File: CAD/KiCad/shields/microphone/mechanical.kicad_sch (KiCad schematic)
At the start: 2 parts

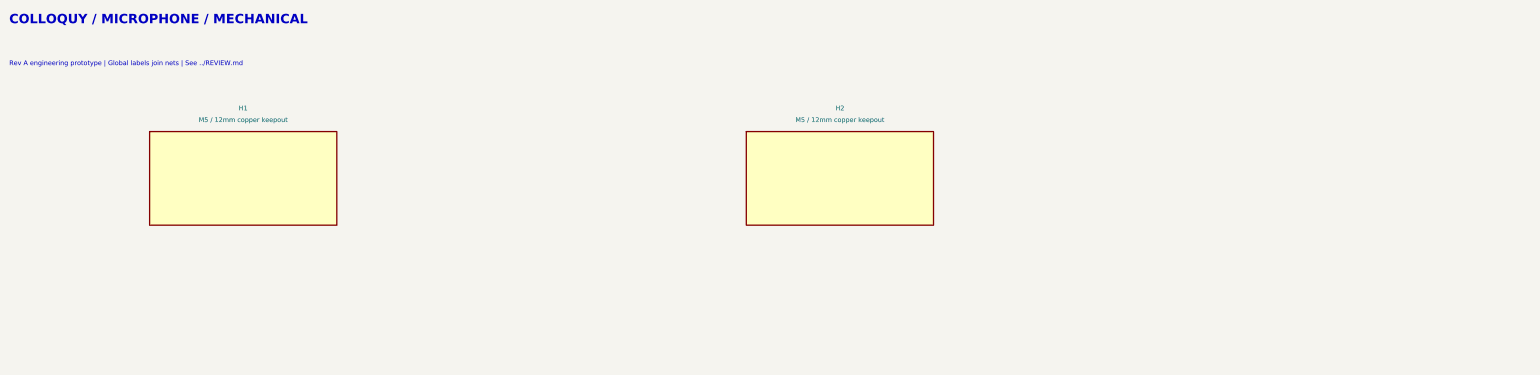
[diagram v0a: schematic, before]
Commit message: Mount the MAX9814 module on a socketed artwork holder
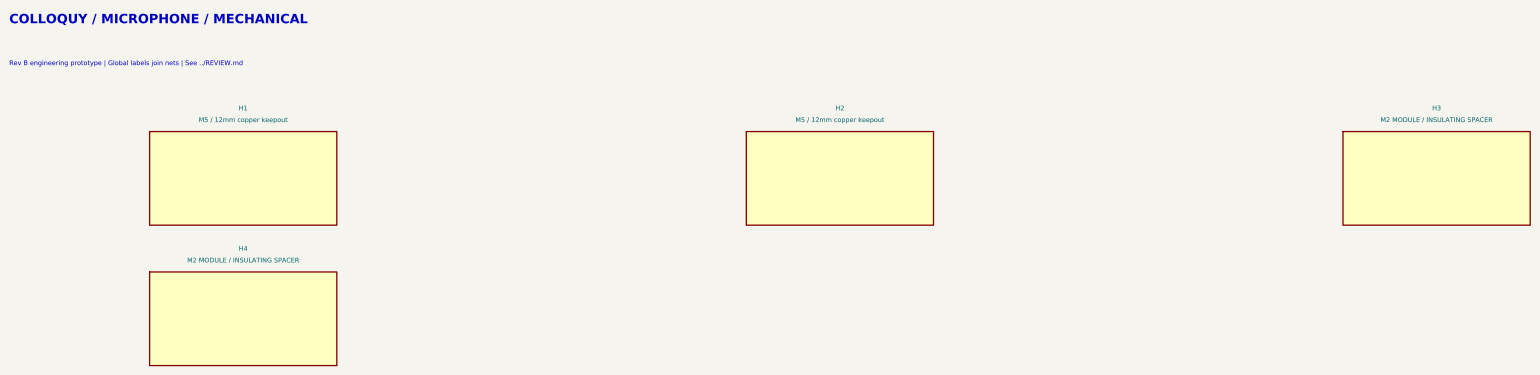
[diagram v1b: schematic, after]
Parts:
- added H3: M2 MODULE / INSULATING SPACER, Shields:MountingHole_2.2mm_M2_Keepout6, symbol Colloquy:H3
- added H4: M2 MODULE / INSULATING SPACER, Shields:MountingHole_2.2mm_M2_Keepout6, symbol Colloquy:H4
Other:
- note added: "Rev B engineering prototype | Global labels join nets | See ../REVIEW.md"
- note removed: "Rev A engineering prototype | Global labels join nets | See ../REVIEW.md"
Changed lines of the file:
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@@
 (kicad_sch (version 20250114) (generator "eeschema") (generator_version "9.0")
  (paper "A3")
-          (title_block (title "microphone / mechanical") (date "2026-10-05") (rev "A-prototype")
+          (title_block (title "microphone / mechanical") (date "2026-10-08") (rev "B-module-holder")
             (company "Colloquy of Mobiles") (comment 1 "Prototype: verify harness polarity and sensor values before connection"))
           (text "COLLOQUY / MICROPHONE / MECHANICAL" (at 15.24 15.24 0) (effects (font (size 2.032 2.032) (bold yes)) (justify left top)))
-(text "Rev A engineering prototype | Global labels join nets | See ../REVIEW.md" (at 15.24 25.4 0) (effects (font (size 1.016 1.016) ) (justify left top)))
+(text "Rev B engineering prototype | Global labels join nets | See ../REVIEW.md" (at 15.24 25.4 0) (effects (font (size 1.016 1.016) ) (justify left top)))
 (symbol (lib_id "Colloquy:H1") (at 66.0400 50.8000 0) (unit 1) (exclude_from_sim no) (in_bom no) (on_board yes) (dnp no)
 (property "Reference" "H1" (at 66.0400 35.5600 0) (effects (font (size 1.016 1.016))  ))
@@
 (property "Description" "" (at 195.5800 50.8000 0) (effects (font (size 1.27 1.27))  (hide yes)))
 (instances (project "microphone" (path "/aa568eb8-4137-509b-b6c6-b3e0a9fa148e/2412fcfe-628e-5f3d-b87f-175f6f93224e" (reference "H2") (unit 1)))))
+(symbol (lib_id "Colloquy:H3") (at 325.1200 50.8000 0) (unit 1) (exclude_from_sim no) (in_bom no) (on_board yes) (dnp no)
+(property "Reference" "H3" (at 325.1200 35.5600 0) (effects (font (size 1.016 1.016))  ))
+(property "Value" "M2 MODULE / INSULATING SPACER" (at 325.1200 38.1000 0) (effects (font (size 1.016 1.016))  ))
+(property "Footprint" "Shields:MountingHole_2.2mm_M2_Keepout6" (at 325.1200 50.8000 0) (effects (font (size 1.27 1.27))  (hide yes)))
+(property "Datasheet" "" (at 325.1200 50.8000 0) (effects (font (size 1.27 1.27))  (hide yes)))
+(property "Description" "" (at 325.1200 50.8000 0) (effects (font (size 1.27 1.27))  (hide yes)))
+(instances (project "microphone" (path "/aa568eb8-4137-509b-b6c6-b3e0a9fa148e/2412fcfe-628e-5f3d-b87f-175f6f93224e" (reference "H3") (unit 1)))))
+(symbol (lib_id "Colloquy:H4") (at 66.0400 81.2800 0) (unit 1) (exclude_from_sim no) (in_bom no) (on_board yes) (dnp no)
+(property "Reference" "H4" (at 66.0400 66.0400 0) (effects (font (size 1.016 1.016))  ))
+(property "Value" "M2 MODULE / INSULATING SPACER" (at 66.0400 68.5800 0) (effects (font (size 1.016 1.016))  ))
+(property "Footprint" "Shields:MountingHole_2.2mm_M2_Keepout6" (at 66.0400 81.2800 0) (effects (font (size 1.27 1.27))  (hide yes)))
+(property "Datasheet" "" (at 66.0400 81.2800 0) (effects (font (size 1.27 1.27))  (hide yes)))
+(property "Description" "" (at 66.0400 81.2800 0) (effects (font (size 1.27 1.27))  (hide yes)))
+(instances (project "microphone" (path "/aa568eb8-4137-509b-b6c6-b3e0a9fa148e/2412fcfe-628e-5f3d-b87f-175f6f93224e" (reference "H4") (unit 1)))))
           (embedded_fonts no))
